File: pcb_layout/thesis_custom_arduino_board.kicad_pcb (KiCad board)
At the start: 2 copper layers, 73.3 x 86.4 mm, 36 parts, among them J1 POWER, J2 USB to TTL, J3 ICSP, J4 VSupply, J5 6-channel Relay, J6 VSupply, J7 Light Sensor, J8 I2C Device, J9 RPi Connector, M1 TXB0104, M2 TB6612FNG, M3 GY-906-BCC, M4 JSN-SR04T, SW1 Reset SW, U1 ATmega328P-P, U2 LM7805, U3 LM317, Y1 16MHz

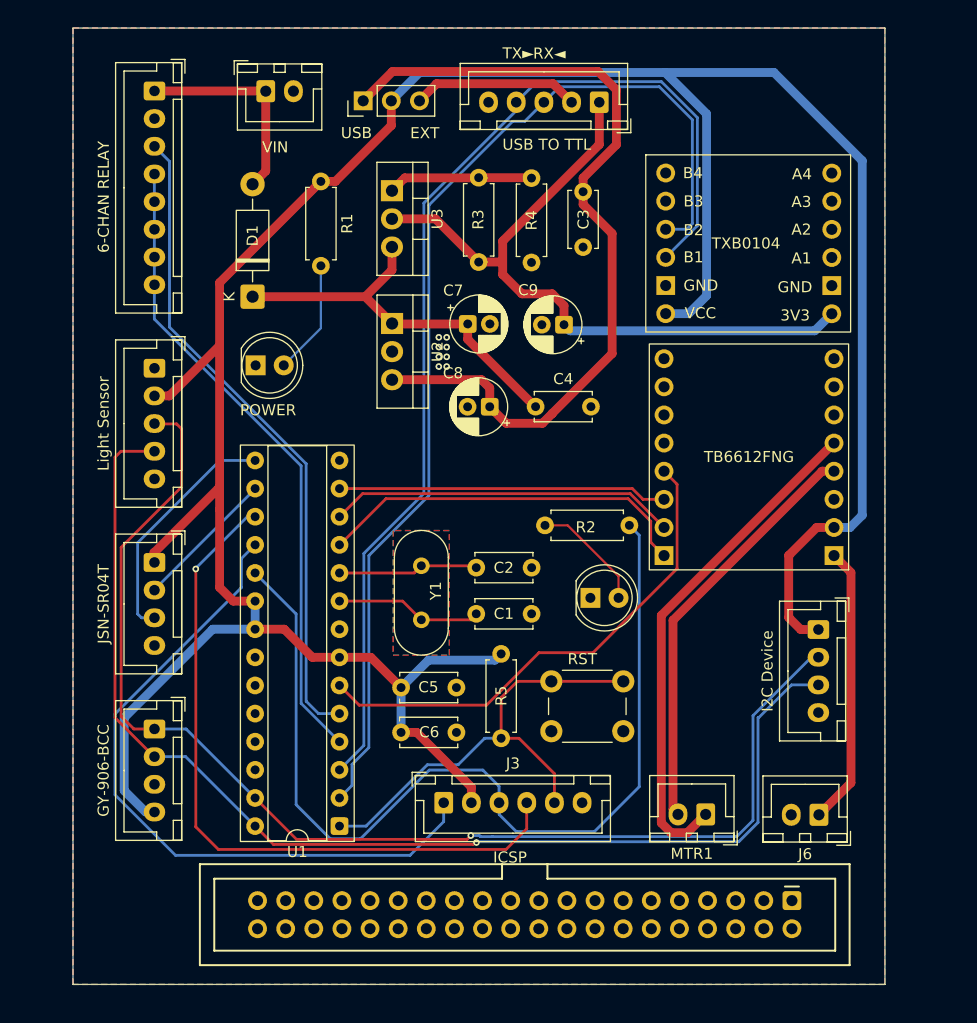
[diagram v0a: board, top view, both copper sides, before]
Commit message: Added: Line detector module pins
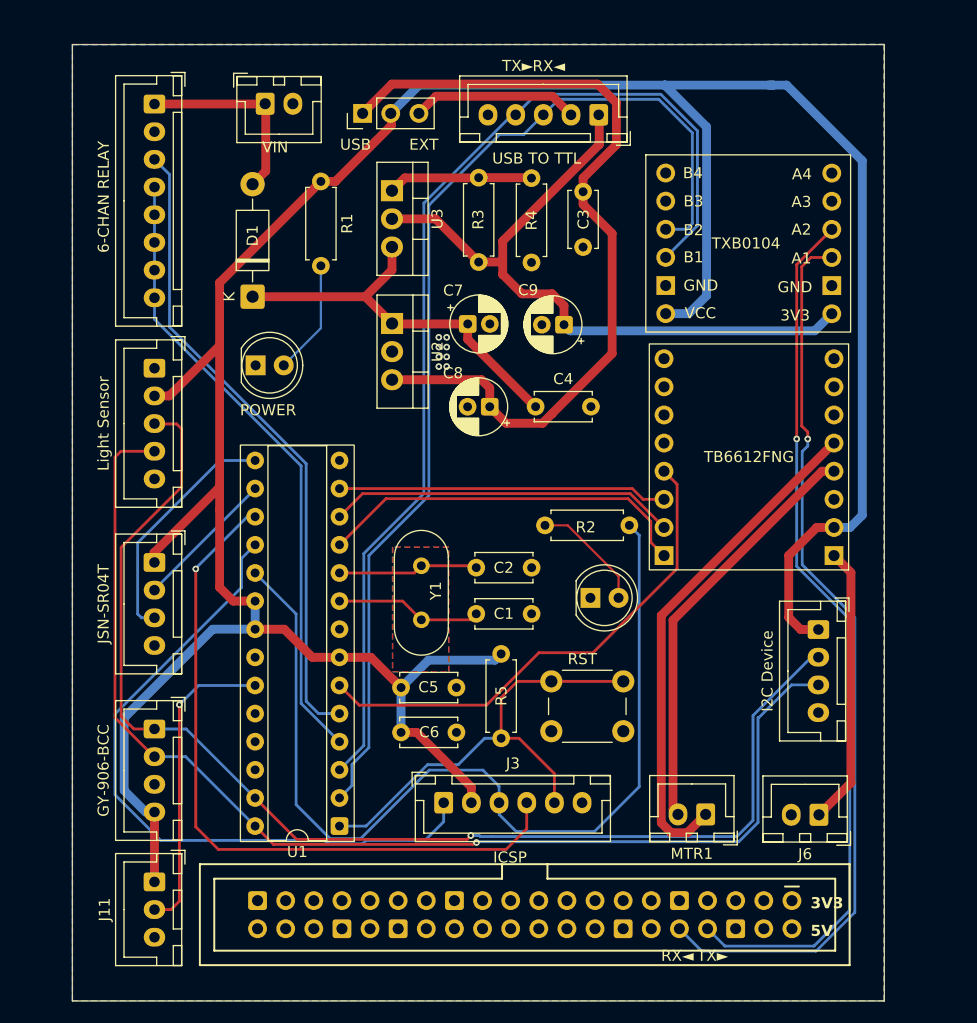
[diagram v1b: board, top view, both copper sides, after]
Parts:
- added J11: LN DETECT, Connector_JST:JST_XH_B3B-XH-A_1x03_P2.50mm_Vertical, F.Cu at (129.8, 150.8)
- moved J5 1.18 mm to (129.8, 80.5)
- moved J1 1.14 mm to (148.6, 81.3)
- moved J4 1.14 mm to (139.8, 80.5)
- moved J2 1.14 mm to (169.9, 81.5)
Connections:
- J9 pad 1: (no net) -> unconnected-(J9-2Pin_a1-Pad1)
- J9 pad 10: (no net) -> /RPI_RXD
- J9 pad 11: (no net) -> unconnected-(J9-Pin_a6-Pad11)
- J9 pad 12: (no net) -> unconnected-(J9-Pin_b6-Pad12)
- J9 pad 13: (no net) -> unconnected-(J9-Pin_a7-Pad13)
- J9 pad 14: (no net) -> unconnected-(J9-Pin_b7-Pad14)
- J9 pad 15: (no net) -> unconnected-(J9-1Pin_a8-Pad15)
- J9 pad 16: (no net) -> unconnected-(J9-Pin_b8-Pad16)
- J9 pad 17: (no net) -> unconnected-(J9-Pin_a9-Pad17)
- J9 pad 18: (no net) -> unconnected-(J9-Pin_b9-Pad18)
- J9 pad 19: (no net) -> unconnected-(J9-Pin_a10-Pad19)
- J9 pad 2: (no net) -> unconnected-(J9-Pin_b1-Pad2)
- J9 pad 20: (no net) -> unconnected-(J9-Pin_b10-Pad20)
- J9 pad 21: (no net) -> unconnected-(J9-Pin_a11-Pad21)
- J9 pad 22: (no net) -> unconnected-(J9-Pin_b11-Pad22)
- J9 pad 23: (no net) -> unconnected-(J9-Pin_a12-Pad23)
- J9 pad 24: (no net) -> unconnected-(J9-Pin_b12-Pad24)
- J9 pad 25: (no net) -> unconnected-(J9-Pin_a13-Pad25)
- J9 pad 26: (no net) -> unconnected-(J9-Pin_b13-Pad26)
- J9 pad 27: (no net) -> unconnected-(J9-Pin_a14-Pad27)
- J9 pad 28: (no net) -> unconnected-(J9-Pin_b14-Pad28)
- J9 pad 29: (no net) -> unconnected-(J9-Pin_a15-Pad29)
- J9 pad 3: (no net) -> unconnected-(J9-Pin_a2-Pad3)
- J9 pad 30: (no net) -> unconnected-(J9-Pin_b15-Pad30)
- J9 pad 31: (no net) -> unconnected-(J9-Pin_a16-Pad31)
- J9 pad 32: (no net) -> unconnected-(J9-Pin_b16-Pad32)
- J9 pad 33: (no net) -> unconnected-(J9-Pin_a17-Pad33)
- J9 pad 34: (no net) -> unconnected-(J9-Pin_b17-Pad34)
- J9 pad 35: (no net) -> unconnected-(J9-Pin_a18-Pad35)
- J9 pad 36: (no net) -> unconnected-(J9-Pin_b18-Pad36)
- J9 pad 37: (no net) -> unconnected-(J9-Pin_a19-Pad37)
- J9 pad 38: (no net) -> unconnected-(J9-Pad38)
- J9 pad 39: (no net) -> unconnected-(J9-Pin_a20-Pad39)
- J9 pad 4: (no net) -> unconnected-(J9-Pin_b2-Pad4)
- J9 pad 40: (no net) -> unconnected-(J9-Pin_b20-Pad40)
- J9 pad 5: (no net) -> unconnected-(J9-Pin_a3-Pad5)
- J9 pad 6: (no net) -> unconnected-(J9-Pin_b3-Pad6)
- J9 pad 7: (no net) -> unconnected-(J9-Pin_a4-Pad7)
- J9 pad 8: (no net) -> /RPI_TXD
- J9 pad 9: (no net) -> unconnected-(J9-Pin_a5-Pad9)
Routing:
- net /RPI_RXD: track 0.00 -> 81.9 mm, vias 0 -> 1
- net /RPI_TXD: track 0.00 -> 79.6 mm, vias 0 -> 1
- net /A0: track 0.00 -> 27.9 mm, vias 0 -> 1
- net VCC: track 260.0 -> 264.0 mm
- net /RXD: track 98.3 -> 96.7 mm
- net /D2: track 58.2 -> 57.0 mm
- net /D3: track 59.3 -> 58.1 mm
- net +3.3V: track 64.3 -> 63.1 mm
- net +5V: track 75.9 -> 74.8 mm
- net VDC: track 19.0 -> 17.9 mm
- net /TXD: track 99.2 -> 98.3 mm
- net /D12: track 62.7 -> 61.9 mm
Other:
- board text added: "3V3"
- board text added: "5V"

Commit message: PCB: Added connectors for buttons and fixed connectors
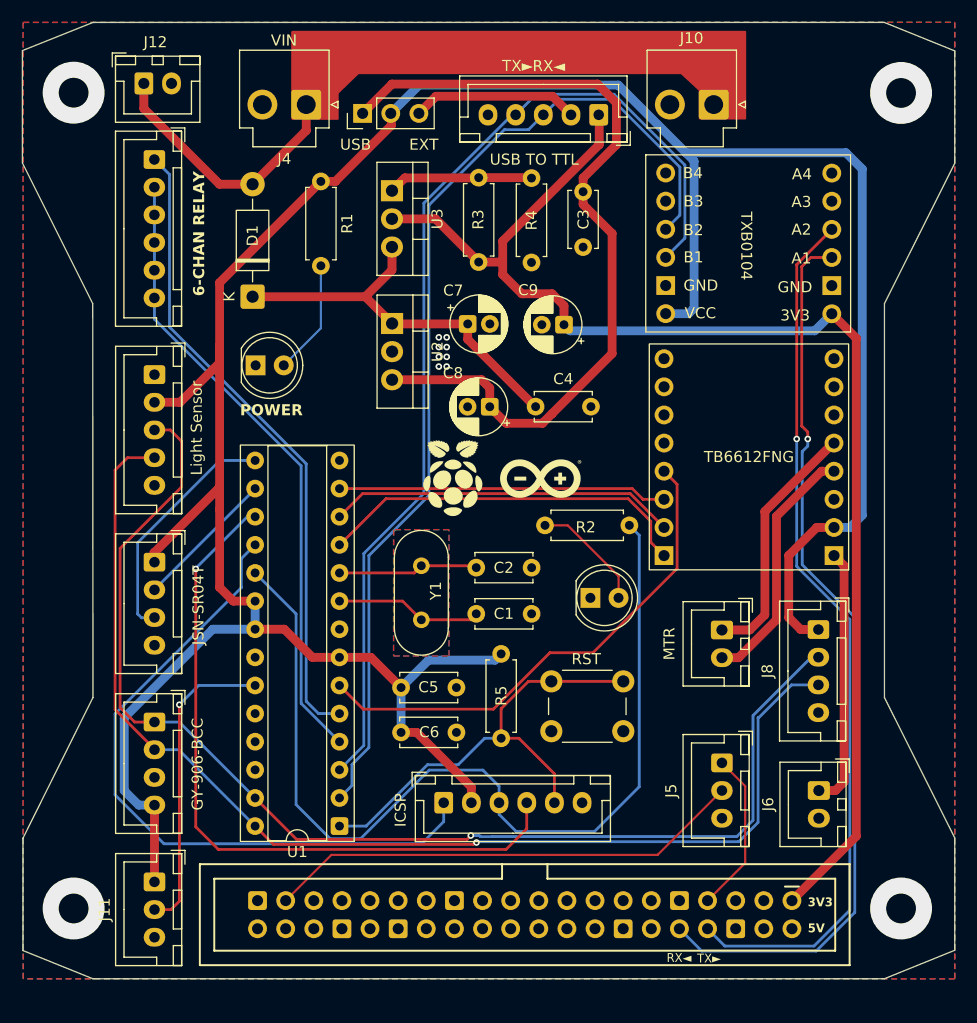
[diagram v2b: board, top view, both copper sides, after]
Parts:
- added J10: RPI VIN, Connector_JST:JST_VH_B2P-VH-B_1x02_P3.96mm_Vertical, F.Cu at (180.3, 80.5)
- added J12: RELAY VIN, Connector_JST:JST_XH_B2B-XH-A_1x02_P2.50mm_Vertical, F.Cu at (128.8, 78.6)
- added J13: 6-CHANNEL RELAY, Connector_JST:JST_XH_B6B-XH-A_1x06_P2.50mm_Vertical, F.Cu at (129.7, 85.5)
- J4: footprint Connector_JST:JST_XH_B2B-XH-A_1x02_P2.50mm_Vertical -> Connector_JST:JST_VH_B2P-VH-B_1x02_P3.96mm_Vertical
- J5: value 6-channel Relay -> Physical Buttons; footprint Connector_JST:JST_XH_B8B-XH-A_1x08_P2.50mm_Vertical -> Connector_JST:JST_XH_B3B-XH-A_1x03_P2.50mm_Vertical
- J8: value I2C Device -> J8
- moved J5 78.5 mm to (181.0, 140.0)
- moved MTR 16.7 mm to (181.0, 128.0), turned to -90 degrees
- moved J4 3.71 mm to (143.5, 80.5), turned to 180 degrees
- moved J6 2.19 mm to (189.8, 142.5), turned to -90 degrees
- moved M3 0.63 mm to (129.8, 136.3)
- moved J7 0.58 mm to (129.8, 104.9)
- renumbered MTR1 to MTR
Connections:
- J5 pad 1: VDC -> /BTN1
- J5 pad 2: GND -> /BTN2
- J5 pad 3: /D3 -> GND
- J9 pad 1: unconnected-(J9-2Pin_a1-Pad1) -> +3.3V
- J9 pad 14: unconnected-(J9-Pin_b7-Pad14) -> GND
- J9 pad 25: unconnected-(J9-Pin_a13-Pad25) -> GND
- J9 pad 30: unconnected-(J9-Pin_b15-Pad30) -> GND
- J9 pad 34: unconnected-(J9-Pin_b17-Pad34) -> GND
- J9 pad 37: unconnected-(J9-Pin_a19-Pad37) -> /BTN2
- J9 pad 39: unconnected-(J9-Pin_a20-Pad39) -> GND
- J9 pad 6: unconnected-(J9-Pin_b3-Pad6) -> GND
- J9 pad 7: unconnected-(J9-Pin_a4-Pad7) -> /BTN1
- J9 pad 9: unconnected-(J9-Pin_a5-Pad9) -> GND
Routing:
- net +3.3V: track 63.1 -> 119.5 mm
- net /BTN2: track 0.00 -> 43.5 mm
- net /mtr_l2: track 45.8 -> 22.6 mm
- net /mtr_l1: track 37.8 -> 22.6 mm
- net /BTN1: track 0.00 -> 14.7 mm
- net VCC: track 264.0 -> 257.1 mm
- net VDC: track 17.9 -> 24.2 mm
- net /RXD: track 96.7 -> 92.2 mm
- net /TXD: track 98.3 -> 94.8 mm
- net +12V: track 25.4 -> 23.5 mm
- net /A4: track 110.8 -> 109.7 mm
- net /A5: track 106.7 -> 105.7 mm
- net /RST: track 41.9 -> 41.4 mm
- net (no net): vias 0 -> 4
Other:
- board size 73.3 x 86.4 mm -> 84.2 x 86.4 mm
- board text added: "Giant Freshwater Prawn PL Counting System Controller Board"

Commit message: PCB layout: Revision 3.0
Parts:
- added J14: DSI VIN, Connector_JST:JST_XH_B2B-XH-A_1x02_P2.50mm_Vertical, F.Cu at (178.6, 135.9)
- J8: value J8 -> I2C Device
- moved J5 6.30 mm to (175.8, 143.6), turned to 0 degrees
- moved MTR1 2.43 mm to (178.6, 127.8), turned to 0 degrees
- renumbered MTR to MTR1
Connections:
- U1 pad 14: /D8 -> unconnected-(U1-PB0-Pad14)
- U1 pad 24: /A1 -> unconnected-(U1-PC1-Pad24)
- U1 pad 25: /A2 -> unconnected-(U1-PC2-Pad25)
- U1 pad 26: /A3 -> unconnected-(U1-PC3-Pad26)
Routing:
- net VDC: track 24.2 -> 82.2 mm
- net /mtr_l1: track 22.6 -> 19.8 mm
- net /BTN2: track 43.5 -> 41.3 mm
- net /mtr_l2: track 22.6 -> 24.0 mm
- net VCC: track 257.1 -> 256.2 mm
- net /BTN1: track 14.7 -> 14.0 mm
